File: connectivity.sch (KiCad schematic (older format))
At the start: 0 parts

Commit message: Schematic: Xbee header
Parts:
- added R? (x2): 330, symbol R_Small
- added R?: 50k, symbol R_Small
- added SW?: SW_PUSH, symbol SW_PUSH
- added U?: XBee_Header, symbol XBee_Header
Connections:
- new net: R?.2, U?.2 (DOUT)
- new net: R?.2, U?.3 (DIN/~CONFIG)
- new net: R?.2, SW?.2, U?.5 (~RESET)
- new net +3V3: R?.1, U?.1 (VCC)
- new net GND: SW?.1, U?.10 (GND)
- new net XBEE_CTS: U?.12 (~CTS~/DIO7)
- new net XBEE_DTR: U?.9 (~DTR~/SLEEP_RQ/DI8)
- new net XBEE_RTS: U?.16 (~RTS~/AD6/DIO6)
- new net XBEE_RX: R?.1
- new net XBEE_TX: R?.1
- no-connect marks 0 -> 12
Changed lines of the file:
@@
 $Descr A4 11693 8268
 encoding utf-8
-Sheet 1 4
+Sheet 2 4
 Title ""
 Date ""
@@
 Comment4 ""
 $EndDescr
+$Comp
+L XBee_Header U?
+U 1 1 55A68758
+P 3700 2850
+F 0 "U?" H 3100 2100 60  0000 C CNN
+F 1 "XBee_Header" H 3700 3600 60  0000 C CNN
+F 2 "" H 3450 2850 60  0000 C CNN
+F 3 "" H 3450 2850 60  0000 C CNN
+	1    3700 2850
+	1    0    0    -1
+$EndComp
+Wire Wire Line
+	4600 3350 4550 3350
+Wire Wire Line
+	4550 3450 4600 3450
+Text HLabel 4850 3450 2    39   Input ~ 0
+XBEE_RX
+Text HLabel 4850 3350 2    39   Input ~ 0
+XBEE_TX
+Wire Wire Line
+	4850 3450 4800 3450
+Wire Wire Line
+	4800 3350 4850 3350
+$Comp
+L R_Small R?
+U 1 1 55A6893C
+P 4700 3350
+F 0 "R?" V 4750 3425 39  0000 L CNN
+F 1 "330" V 4700 3350 39  0000 C CNN
+F 2 "" H 4700 3350 60  0000 C CNN
+F 3 "" H 4700 3350 60  0000 C CNN
+	1    4700 3350
+	0    1    1    0
+$EndComp
+$Comp
+L R_Small R?
+U 1 1 55A689EB
+P 4700 3450
+F 0 "R?" V 4750 3525 39  0000 L CNN
+F 1 "330" V 4700 3450 39  0000 C CNN
+F 2 "" H 4700 3450 60  0000 C CNN
+F 3 "" H 4700 3450 60  0000 C CNN
+	1    4700 3450
+	0    1    1    0
+$EndComp
+NoConn ~ 4550 2250
+NoConn ~ 4550 2350
+NoConn ~ 4550 2450
+NoConn ~ 4550 2550
+NoConn ~ 4550 2650
+NoConn ~ 4550 2750
+NoConn ~ 4550 2850
+Text HLabel 4600 3050 2    39   Input ~ 0
+XBEE_CTS
+Wire Wire Line
+	4600 2950 4550 2950
+Text HLabel 4600 2950 2    39   Input ~ 0
+XBEE_RTS
+Wire Wire Line
+	4600 3050 4550 3050
+$Comp
+L +3V3 #PWR?
+U 1 1 55A68A9D
+P 2800 2200
+F 0 "#PWR?" H 2800 2050 50  0001 C CNN
+F 1 "+3V3" H 2800 2340 50  0000 C CNN
+F 2 "" H 2800 2200 60  0000 C CNN
+F 3 "" H 2800 2200 60  0000 C CNN
+	1    2800 2200
+	1    0    0    -1
+$EndComp
+Wire Wire Line
+	2800 2200 2800 2250
+Wire Wire Line
+	2800 2250 2850 2250
+NoConn ~ 2850 2450
+NoConn ~ 2850 2650
+NoConn ~ 2850 2850
+NoConn ~ 2850 2950
+NoConn ~ 2850 3150
+$Comp
+L GND #PWR?
+U 1 1 55A68AF1
+P 2800 3500
+F 0 "#PWR?" H 2800 3250 50  0001 C CNN
+F 1 "GND" H 2800 3350 50  0000 C CNN
+F 2 "" H 2800 3500 60  0000 C CNN
+F 3 "" H 2800 3500 60  0000 C CNN
+	1    2800 3500
+	1    0    0    -1
+$EndComp
+Wire Wire Line
+	2800 3500 2800 3450
+Wire Wire Line
+	2800 3450 2850 3450
+$Comp
+L SW_PUSH SW?
+U 1 1 55A68B18
+P 2325 2900
+F 0 "SW?" H 2475 3010 50  0000 C CNN
+F 1 "SW_PUSH" H 2325 2820 50  0000 C CNN
+F 2 "" H 2325 2900 60  0000 C CNN
+F 3 "" H 2325 2900 60  0000 C CNN
+	1    2325 2900
+	0    -1   -1   0
+$EndComp
+$Comp
+L GND #PWR?
+U 1 1 55A68BA5
+P 2325 3250
+F 0 "#PWR?" H 2325 3000 50  0001 C CNN
+F 1 "GND" H 2325 3100 50  0000 C CNN
+F 2 "" H 2325 3250 60  0000 C CNN
+F 3 "" H 2325 3250 60  0000 C CNN
+	1    2325 3250
+	1    0    0    -1
+$EndComp
+Wire Wire Line
+	2325 3200 2325 3250
+$Comp
+L R_Small R?
+U 1 1 55A68BCB
+P 2325 2375
+F 0 "R?" H 2355 2395 50  0000 L CNN
+F 1 "50k" H 2355 2335 50  0000 L CNN
+F 2 "" H 2325 2375 60  0000 C CNN
+F 3 "" H 2325 2375 60  0000 C CNN
+	1    2325 2375
+	1    0    0    -1
+$EndComp
+Wire Wire Line
+	2325 2475 2325 2550
+Wire Wire Line
+	2325 2550 2325 2600
+Wire Wire Line
+	2325 2550 2850 2550
+Connection ~ 2325 2550
+$Comp
+L +3V3 #PWR?
+U 1 1 55A68C91
+P 2325 2200
+F 0 "#PWR?" H 2325 2050 50  0001 C CNN
+F 1 "+3V3" H 2325 2340 50  0000 C CNN
+F 2 "" H 2325 2200 60  0000 C CNN
+F 3 "" H 2325 2200 60  0000 C CNN
+	1    2325 2200
+	1    0    0    -1
+$EndComp
+Wire Wire Line
+	2325 2200 2325 2275
+Text HLabel 2800 3350 0    39   Input ~ 0
+XBEE_DTR
+Wire Wire Line
+	2800 3350 2850 3350
 $EndSCHEMATC

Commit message: Schematics: PWM
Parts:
- added CONN? (x12): SERVO, symbol SERVO
- added R?: 10k, symbol R_Small
- added U?: PCA9685, symbol PCA9685
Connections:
- net GND: now also CONN?.3 (GND), CONN?.3 (GND), CONN?.3 (GND), CONN?.3 (GND), CONN?.3 (GND), CONN?.3 (GND), CONN?.3 (GND), CONN?.3 (GND), CONN?.3 (GND), CONN?.3 (GND), CONN?.3 (GND), CONN?.3 (GND), U?.1 (A0), U?.14 (VSS), U?.2 (A1), U?.24 (A5), U?.25 (EXTCLK), U?.3 (A2), U?.4 (A3), U?.5 (A4)
- new net +3.3V_A: R?.1, U?.28 (VDD)
- new net I2C2_SCL: U?.26 (SCL)
- new net I2C2_SDA: U?.27 (SDA)
- new net POWER: CONN?.2 (V+), CONN?.2 (V+), CONN?.2 (V+), CONN?.2 (V+), CONN?.2 (V+), CONN?.2 (V+), CONN?.2 (V+), CONN?.2 (V+), CONN?.2 (V+), CONN?.2 (V+), CONN?.2 (V+), CONN?.2 (V+)
- new net PWMGEN_OE: R?.2, U?.23 (~OE)
- new net PWM_0: CONN?.1 (Signal)
- new net PWM_1: CONN?.1 (Signal)
- new net PWM_10: CONN?.1 (Signal), U?.10 (LED4)
- new net PWM_11: CONN?.1 (Signal), U?.11 (LED5)
- new net PWM_2: CONN?.1 (Signal)
- new net PWM_3: CONN?.1 (Signal)
- new net PWM_4: CONN?.1 (Signal)
- new net PWM_5: CONN?.1 (Signal)
- new net PWM_6: CONN?.1 (Signal), U?.6 (LED0)
- new net PWM_7: CONN?.1 (Signal), U?.7 (LED1)
- new net PWM_8: CONN?.1 (Signal), U?.8 (LED2)
- new net PWM_9: CONN?.1 (Signal), U?.9 (LED3)
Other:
- note added: "I2C address: \n0x40\n"
- moved on the sheet: R?, SW?, U?

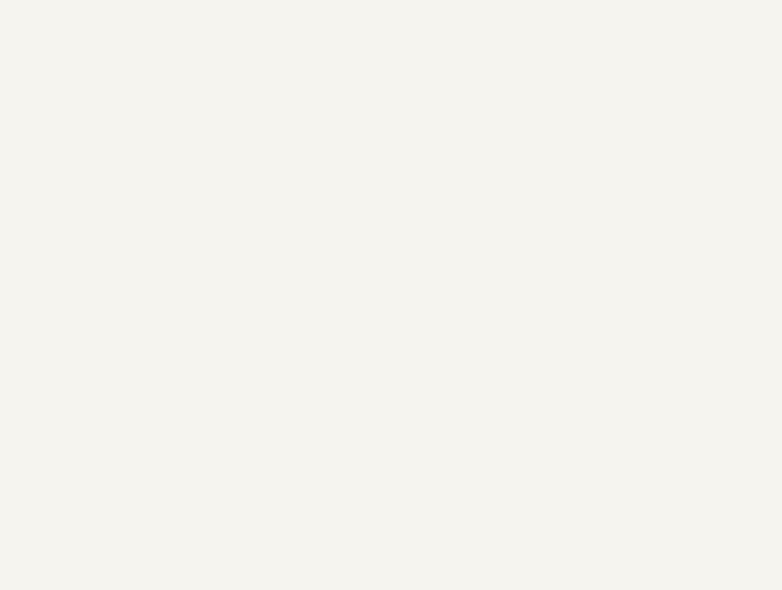
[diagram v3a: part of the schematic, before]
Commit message: Schematics: CAN
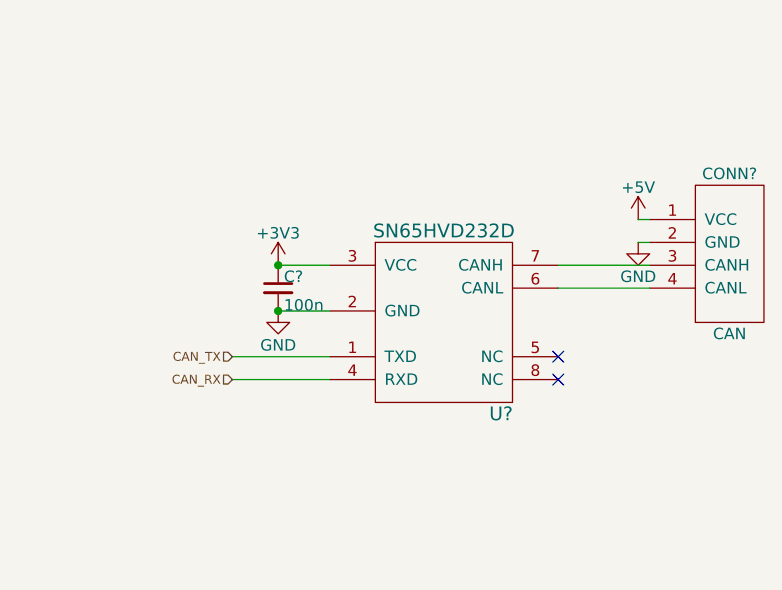
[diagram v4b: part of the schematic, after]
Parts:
- added C?: 100n, symbol C_Small
- added CONN?: CAN, MODULE, symbol CAN
- added U?: SN65HVD232D, symbol SN65HVD232D
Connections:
- net +3V3: now also C?.1, U?.3 (VCC)
- net GND: now also C?.2, CONN?.2 (GND), CONN?.MECH (GND), U?.2 (GND)
- new net: CONN?.4 (CANL), U?.6 (CANL)
- new net: CONN?.3 (CANH), U?.7 (CANH)
- new net +5V: CONN?.1 (VCC)
- new net CAN_RX: U?.4 (RXD)
- new net CAN_TX: U?.1 (TXD)
- no-connect marks 12 -> 14
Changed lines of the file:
@@
 Wire Wire Line
 	3075 1800 3125 1800
+$Comp
+L SN65HVD232D U?
+U 1 1 55AABB00
+P 7700 4850
+F 0 "U?" H 7950 4400 60  0000 C CNN
+F 1 "SN65HVD232D" H 7700 5200 60  0000 C CNN
+F 2 "" H 7700 4850 60  0000 C CNN
+F 3 "" H 7700 4850 60  0000 C CNN
+	1    7700 4850
+	1    0    0    -1
+$EndComp
+$Comp
+L CAN CONN?
+U 1 1 55AABB6D
+P 8950 4600
+F 0 "CONN?" H 8950 4950 50  0000 C CNN
+F 1 "CAN" H 8950 4250 50  0000 C CNN
+F 2 "MODULE" H 9200 4600 50  0001 C CNN
+F 3 "DOCUMENTATION" H 9200 4600 50  0001 C CNN
+	1    8950 4600
+	1    0    0    -1
+$EndComp
+$Comp
+L C_Small C?
+U 1 1 55AABD28
+P 6975 4750
+F 0 "C?" H 7000 4800 50  0000 L CNN
+F 1 "100n" H 7000 4675 50  0000 L CNN
+F 2 "" H 6975 4750 60  0000 C CNN
+F 3 "" H 6975 4750 60  0000 C CNN
+	1    6975 4750
+	1    0    0    -1
+$EndComp
+Wire Wire Line
+	7200 4650 6975 4650
+Wire Wire Line
+	6975 4850 7200 4850
+$Comp
+L GND #PWR?
+U 1 1 55AABF17
+P 6975 4850
+F 0 "#PWR?" H 6975 4600 50  0001 C CNN
+F 1 "GND" H 6975 4700 50  0000 C CNN
+F 2 "" H 6975 4850 60  0000 C CNN
+F 3 "" H 6975 4850 60  0000 C CNN
+	1    6975 4850
+	1    0    0    -1
+$EndComp
+Connection ~ 6975 4850
+Connection ~ 6975 4650
+$Comp
+L +3V3 #PWR?
+U 1 1 55AABF5B
+P 6975 4650
+F 0 "#PWR?" H 6975 4500 50  0001 C CNN
+F 1 "+3V3" H 6975 4790 50  0000 C CNN
+F 2 "" H 6975 4650 60  0000 C CNN
+F 3 "" H 6975 4650 60  0000 C CNN
+	1    6975 4650
+	1    0    0    -1
+$EndComp
+NoConn ~ 8200 5050
+NoConn ~ 8200 5150
+Wire Wire Line
+	8200 4650 8600 4650
+Wire Wire Line
+	8600 4750 8200 4750
+$Comp
+L +5V #PWR?
+U 1 1 55AAC661
+P 8550 4450
+F 0 "#PWR?" H 8550 4300 50  0001 C CNN
+F 1 "+5V" H 8550 4590 50  0000 C CNN
+F 2 "" H 8550 4450 60  0000 C CNN
+F 3 "" H 8550 4450 60  0000 C CNN
+	1    8550 4450
+	1    0    0    -1
+$EndComp
+Wire Wire Line
+	8550 4450 8600 4450
+$Comp
+L GND #PWR?
+U 1 1 55AAC741
+P 8550 4550
+F 0 "#PWR?" H 8550 4300 50  0001 C CNN
+F 1 "GND" H 8550 4400 50  0000 C CNN
+F 2 "" H 8550 4550 60  0000 C CNN
+F 3 "" H 8550 4550 60  0000 C CNN
+	1    8550 4550
+	1    0    0    -1
+$EndComp
+Wire Wire Line
+	8550 4550 8600 4550
+Text HLabel 6775 5050 0    39   Input ~ 0
+CAN_TX
+Wire Wire Line
+	6775 5050 7200 5050
+Text HLabel 6775 5150 0    39   Input ~ 0
+CAN_RX
+Wire Wire Line
+	6775 5150 7200 5150
 $EndSCHEMATC

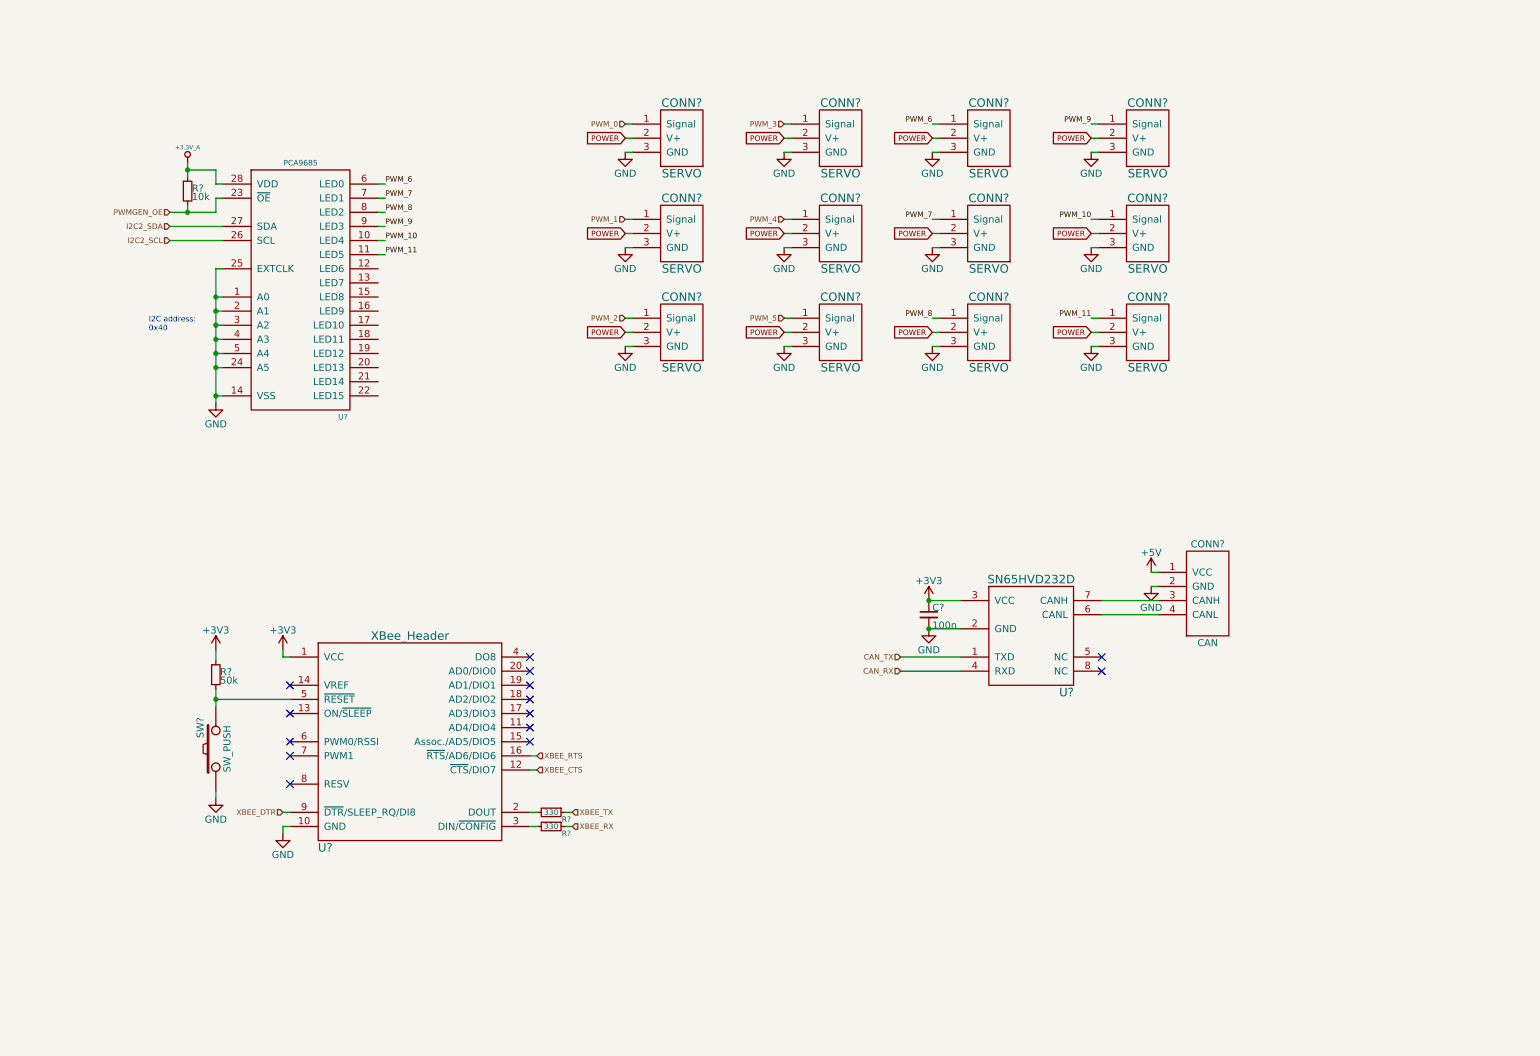
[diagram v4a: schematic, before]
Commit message: Schematics: Additional connectors (ADC, I2C, UART)
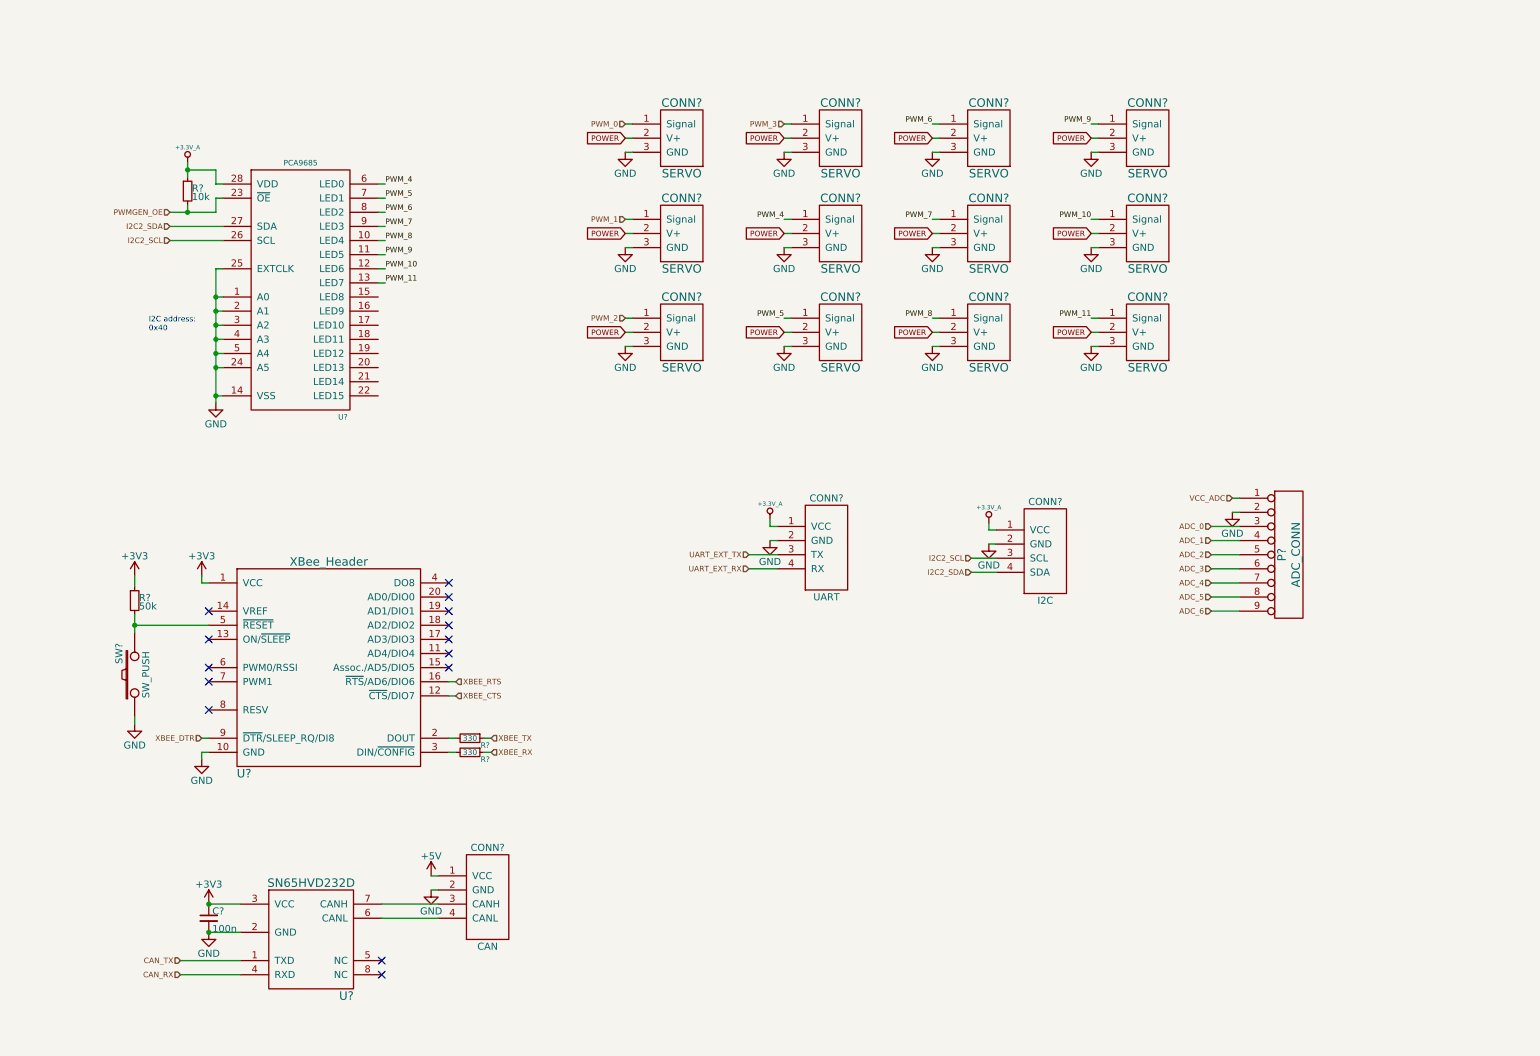
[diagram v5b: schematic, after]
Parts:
- added CONN?: UART, MODULE, symbol UART
- added CONN?: I2C, MODULE, symbol I2C
- added P?: ADC_CONN, symbol CONN_9
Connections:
- net +3.3V_A: now also CONN?.1 (VCC), CONN?.1 (VCC)
- net GND: now also CONN?.2 (GND), CONN?.2 (GND), CONN?.MECH (GND), CONN?.MECH (GND), P?.2 (P2)
- net I2C2_SCL: now also CONN?.3 (SCL)
- net I2C2_SDA: now also CONN?.4 (SDA)
- net PWM_10: now also U?.12 (LED6); no longer U?.10 (LED4)
- net PWM_11: now also U?.13 (LED7); no longer U?.11 (LED5)
- net PWM_4: now also U?.6 (LED0)
- net PWM_5: now also U?.7 (LED1)
- net PWM_6: now also U?.8 (LED2); no longer U?.6 (LED0)
- net PWM_7: now also U?.9 (LED3); no longer U?.7 (LED1)
- net PWM_8: now also U?.10 (LED4); no longer U?.8 (LED2)
- net PWM_9: now also U?.11 (LED5); no longer U?.9 (LED3)
- new net ADC_0: P?.3 (P3)
- new net ADC_1: P?.4 (P4)
- new net ADC_2: P?.5 (P5)
- new net ADC_3: P?.6 (P6)
- new net ADC_4: P?.7 (P7)
- new net ADC_5: P?.8 (P8)
- new net ADC_6: P?.9 (P9)
- new net UART_EXT_RX: CONN?.4 (RX)
- new net UART_EXT_TX: CONN?.3 (TX)
- new net VCC_ADC: P?.1 (P1)
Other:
- moved on the sheet: C?, CONN?, R?, SW?, U?

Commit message: Schematics: RTC
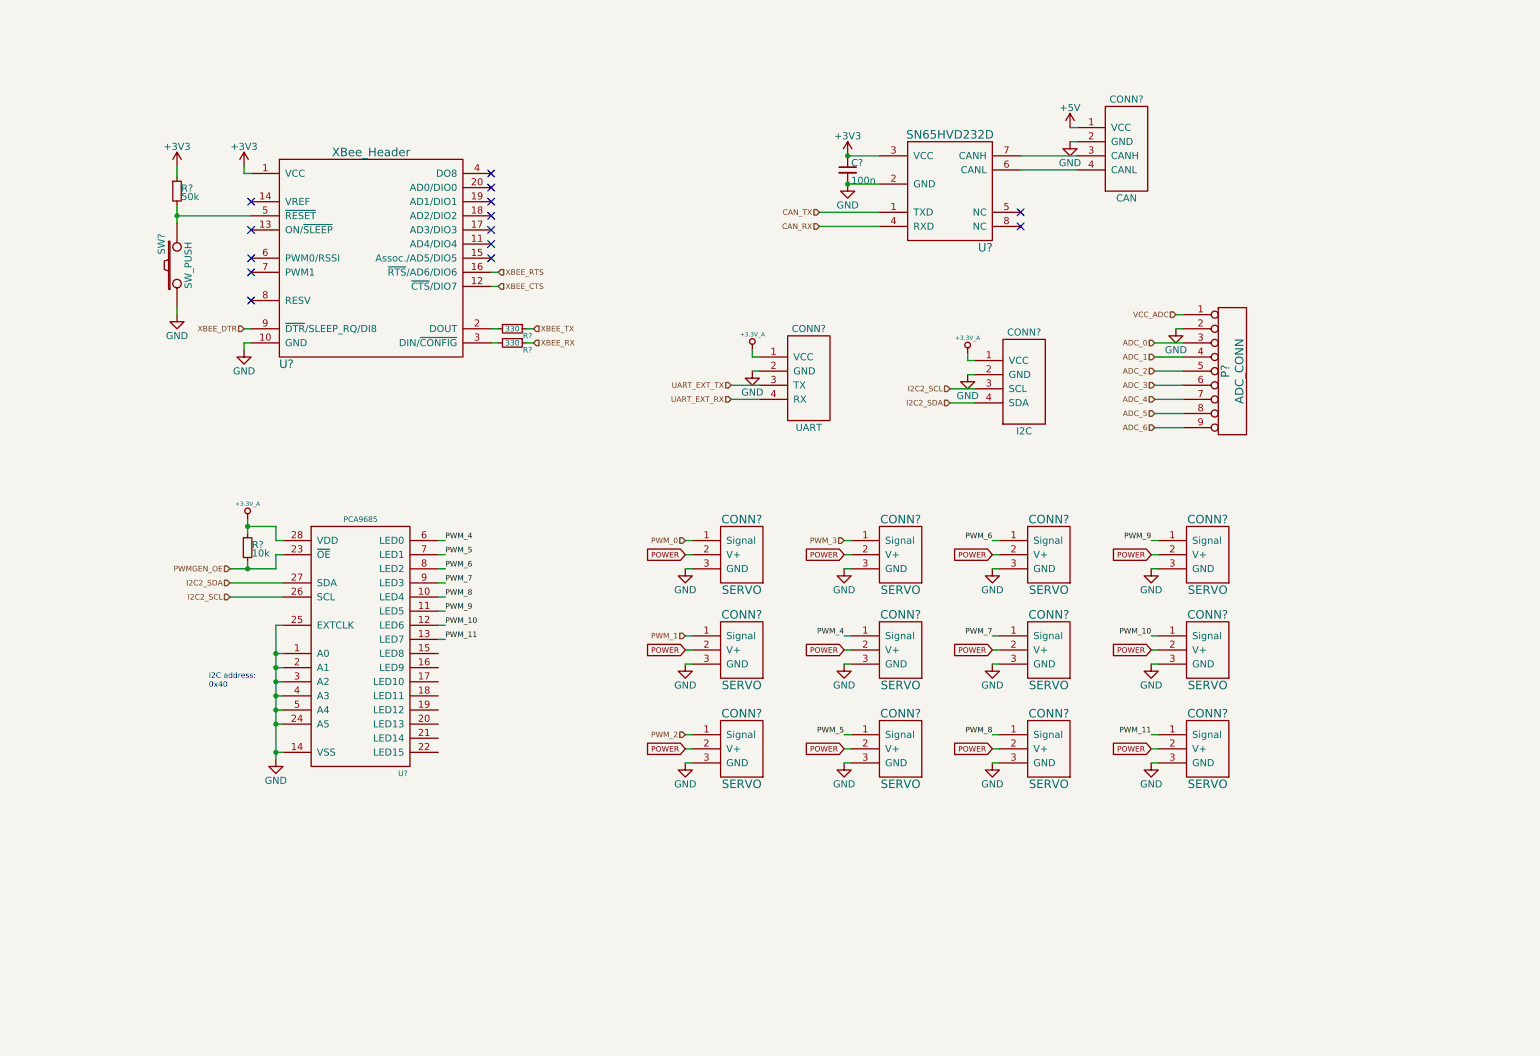
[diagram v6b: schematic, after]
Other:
- moved on the sheet: C?, CONN?, P?, R?, SW?, U?
